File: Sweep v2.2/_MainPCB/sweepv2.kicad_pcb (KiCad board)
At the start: 2 copper layers, 216.9 x 86.9 mm, 58 parts, among them J1 AudioJack4dpb, J2 AudioJack4dpb, SW1 SW_Push, SW10 SW_Push, SW11 SW_Push, SW11_r1 SW_Push, SW12 SW_Push, SW12_r1 SW_Push, SW13_r1 SW_Push, SW14 SW_Push, SW15 SW_Push, SW15_r1 SW_Push, SW16 SW_Push, SW16_r1 SW_Push, SW17 SW_Push, SW17_r1 SW_Push, SW18 SW_Push, SW18_r1 SW_Push, SW2 SW_Push, SW20 SW_Push, SW21 SW_Push, SW2_r1 SW_Push, SW3 SW_Push, SW3_r1 SW_Push, SW4 SW_Push, SW4_r1 SW_Push, SW5 SW_Push, SW5_r1 SW_Push, SW6 SW_Push, SW6_r1 SW_Push, SW7 SW_Push, SW7_r1 SW_Push, SW8 SW_Push, SW8_r1 SW_Push, SW9 SW_Push, SW9_r1 SW_Push, U1 ProMicro-kbd, U2 ProMicro-kbd

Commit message: lots of worky
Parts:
- added G***: LOGO, Kailh:ferris_broom, F.Cu at (175.6, 84.1)

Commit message: routed one trace nicer
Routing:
- net Switch12_r: track 123.7 -> 130.9 mm
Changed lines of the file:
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@@
   (segment (start 22.706 63.754) (end 26.075 67.123) (width 0.15) (layer "B.Cu") (net 28))
   (segment (start 34.69632 83.275) (end 42.327208 83.275) (width 0.15) (layer "B.Cu") (net 28))
-  (segment (start 56.3 97.6) (end 60.4 97.6) (width 0.15) (layer "F.Cu") (net 29))
-  (segment (start 49.800736 97.3) (end 56 97.3) (width 0.15) (layer "F.Cu") (net 29))
-  (segment (start 60.4 97.6) (end 64.075 96.675) (width 0.15) (layer "F.Cu") (net 29))
-  (segment (start 24.65 73.824264) (end 24.65 83.399264) (width 0.15) (layer "F.Cu") (net 29))
-  (segment (start 24.65 83.399264) (end 24.05 83.999264) (width 0.15) (layer "F.Cu") (net 29))
-  (segment (start 45.625736 93.125) (end 49.800736 97.3) (width 0.15) (layer "F.Cu") (net 29))
-  (segment (start 24.925 68.513) (end 24.925 73.549264) (width 0.15) (layer "F.Cu") (net 29))
-  (segment (start 93.35 92) (end 120.204999 89.809001) (width 0.15) (layer "F.Cu") (net 29))
-  (segment (start 82.2 93.6) (end 93.35 92) (width 0.15) (layer "F.Cu") (net 29))
-  (segment (start 22.706 66.294) (end 24.925 68.513) (width 0.15) (layer "F.Cu") (net 29))
-  (segment (start 30.449264 93.125) (end 45.625736 93.125) (width 0.15) (layer "F.Cu") (net 29))
-  (segment (start 64.075 96.675) (end 75.475 94.825) (width 0.15) (layer "F.Cu") (net 29))
-  (segment (start 24.05 86.725736) (end 30.449264 93.125) (width 0.15) (layer "F.Cu") (net 29))
-  (segment (start 75.475 94.825) (end 82.2 93.6) (width 0.15) (layer "F.Cu") (net 29))
-  (segment (start 24.925 73.549264) (end 24.65 73.824264) (width 0.15) (layer "F.Cu") (net 29))
-  (segment (start 24.05 83.999264) (end 24.05 86.725736) (width 0.15) (layer "F.Cu") (net 29))
-  (segment (start 56 97.3) (end 56.3 97.6) (width 0.15) (layer "F.Cu") (net 29))
-  (segment (start 120.204999 89.809001) (end 120.732 89.282) (width 0.15) (layer "F.Cu") (net 29))
+  (segment (start 24.65 73.824264) (end 24.925 73.549264) (width 0.15) (layer "F.Cu") (net 29))
+  (segment (start 24.05 83.999264) (end 24.65 83.399264) (width 0.15) (layer "F.Cu") (net 29))
+  (segment (start 42.83 86.8) (end 37.572132 92.057868) (width 0.15) (layer "F.Cu") (net 29))
+  (segment (start 24.65 83.399264) (end 24.65 73.824264) (width 0.15) (layer "F.Cu") (net 29))
+  (segment (start 120.732 89.282) (end 117.49 86.04) (width 0.15) (layer "F.Cu") (net 29))
+  (segment (start 52.373528 86.8) (end 42.83 86.8) (width 0.15) (layer "F.Cu") (net 29))
+  (segment (start 117.49 82.5106) (end 115.7497 80.7703) (width 0.15) (layer "F.Cu") (net 29))
+  (segment (start 24.925 68.513) (end 22.706 66.294) (width 0.15) (layer "F.Cu") (net 29))
+  (segment (start 115.7497 80.7703) (end 58.403228 80.7703) (width 0.15) (layer "F.Cu") (net 29))
+  (segment (start 29.382132 92.057868) (end 24.05 86.725736) (width 0.15) (layer "F.Cu") (net 29))
+  (segment (start 24.925 73.549264) (end 24.925 68.513) (width 0.15) (layer "F.Cu") (net 29))
+  (segment (start 58.403228 80.7703) (end 52.373528 86.8) (width 0.15) (layer "F.Cu") (net 29))
+  (segment (start 37.572132 92.057868) (end 29.382132 92.057868) (width 0.15) (layer "F.Cu") (net 29))
+  (segment (start 24.05 86.725736) (end 24.05 83.999264) (width 0.15) (layer "F.Cu") (net 29))
+  (segment (start 117.49 86.04) (end 117.49 82.5106) (width 0.15) (layer "F.Cu") (net 29))
   (segment (start 23.75 86.85) (end 35.375 98.475) (width 0.15) (layer "F.Cu") (net 30))
   (segment (start 35.375 99.925) (end 38.65955 103.20955) (width 0.15) (layer "F.Cu") (net 30))

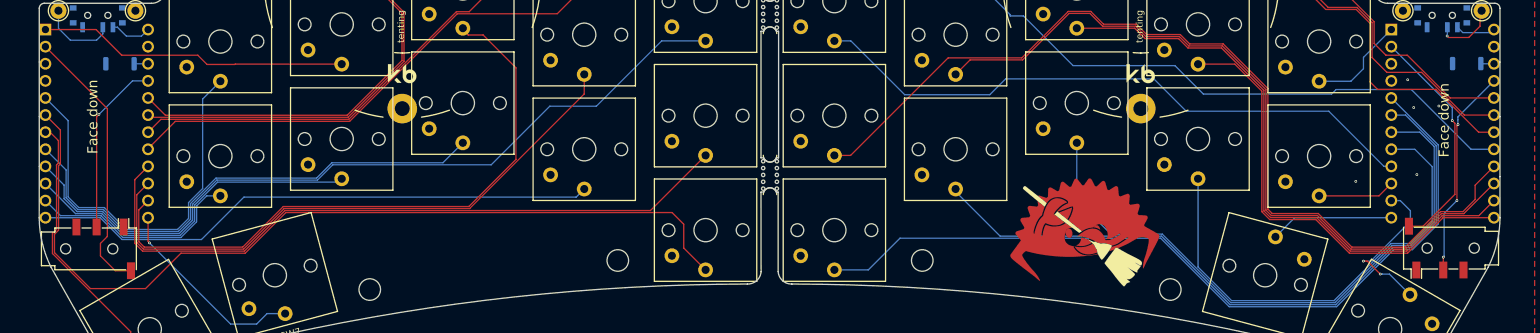
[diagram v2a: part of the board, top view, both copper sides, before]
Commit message: some adjustments and stuff, changed my mind on some footprints and also missed some stuff I used for alignment and checking
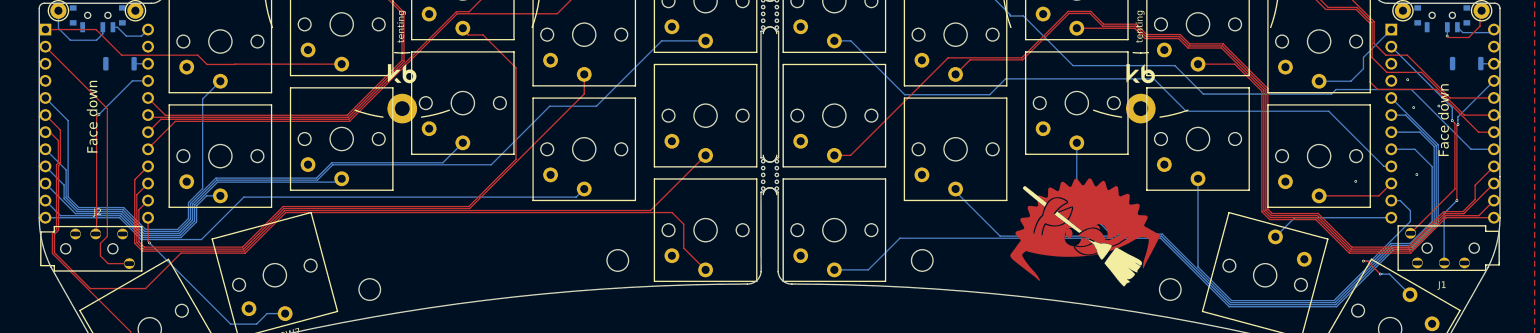
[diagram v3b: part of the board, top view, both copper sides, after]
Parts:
- J1, J2: footprint Connector_Audio:Jack_3.5mm_PJ320D_Horizontal -> env_extra:PJ-320A
- moved J1 8.76 mm to (238.6, 88.2)
- moved J2 8.75 mm to (22.0, 84.0)
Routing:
- net Switch18_r: track 40.7 -> 40.1 mm
- net vcc: vias 4 -> 3
